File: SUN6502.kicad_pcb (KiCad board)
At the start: 4 copper layers, 221 x 179 mm, 52 parts, among them J1 Barrel_Jack_MountingPin, J2 6-5530843-5, J3 6-5530843-5, J4 DE9_Socket, SW1 RESET, SW2 Power Switch, U1 W65C02SxP, U10 MAX232, U11 74LS00, U2 KM62256CLP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

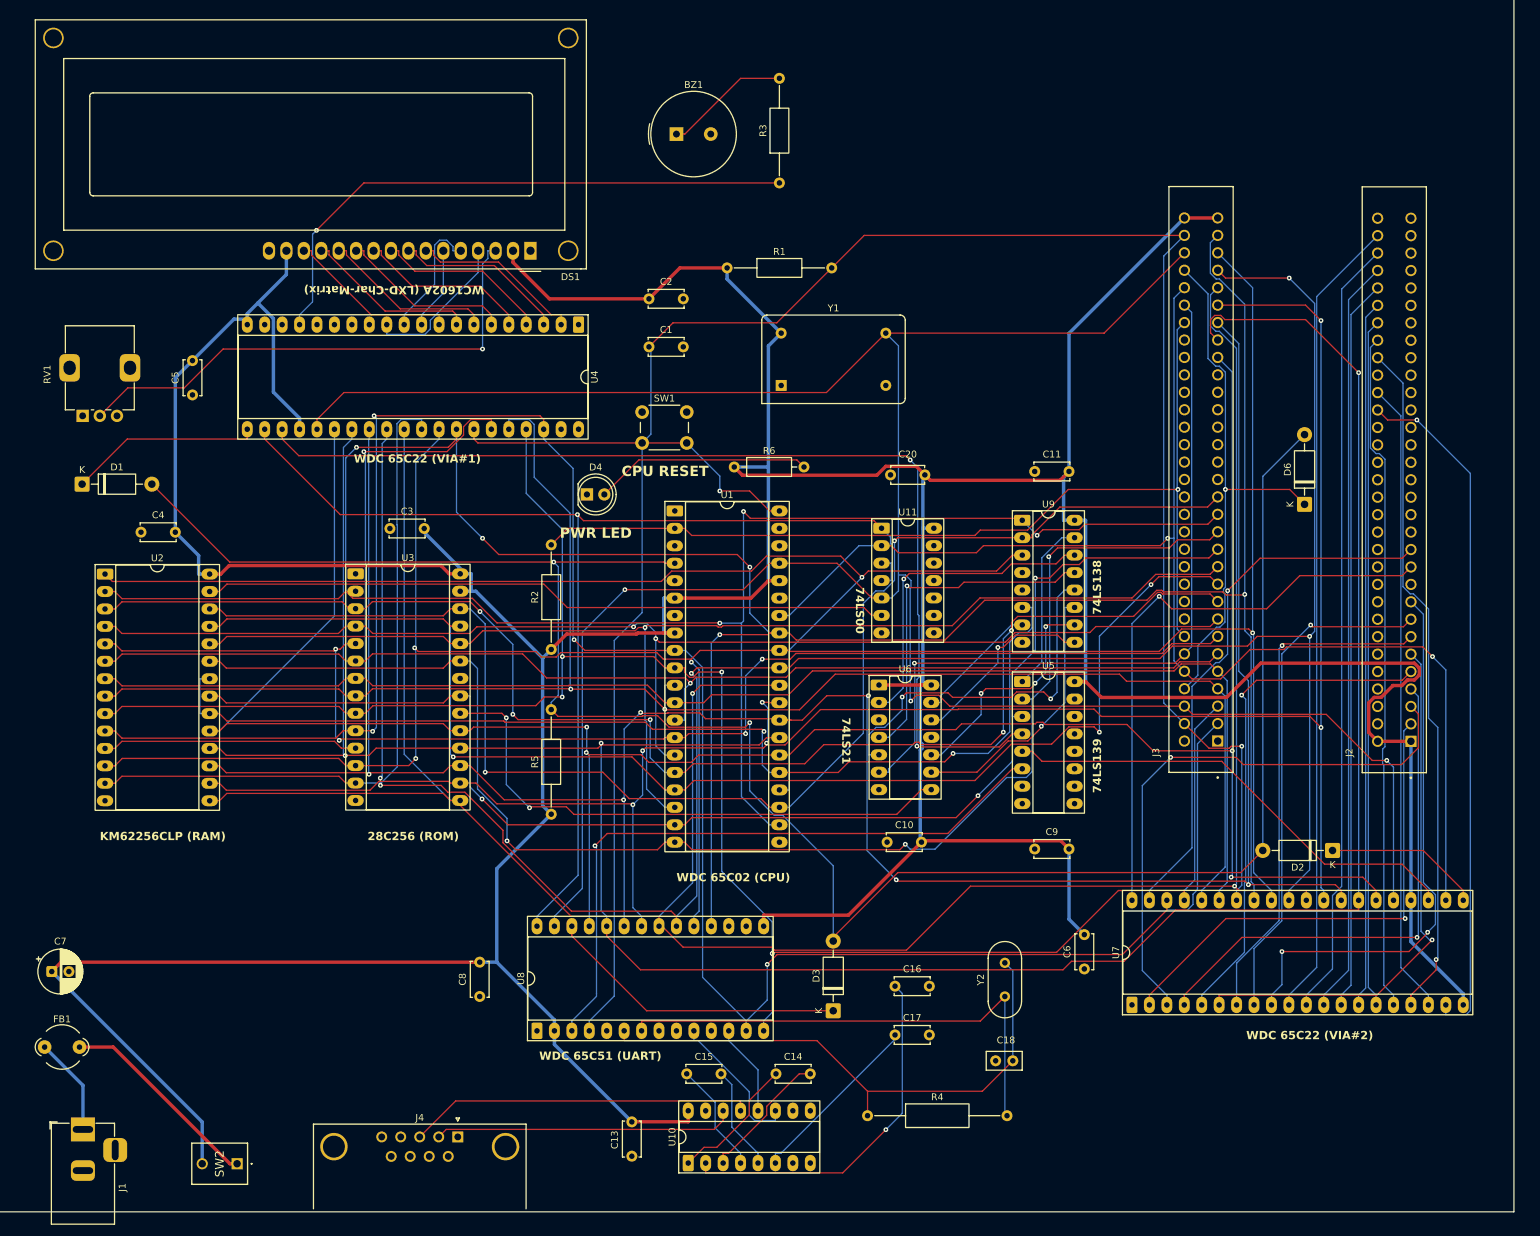
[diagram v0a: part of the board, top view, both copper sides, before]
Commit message: updates, changed ROM socket into ZIF
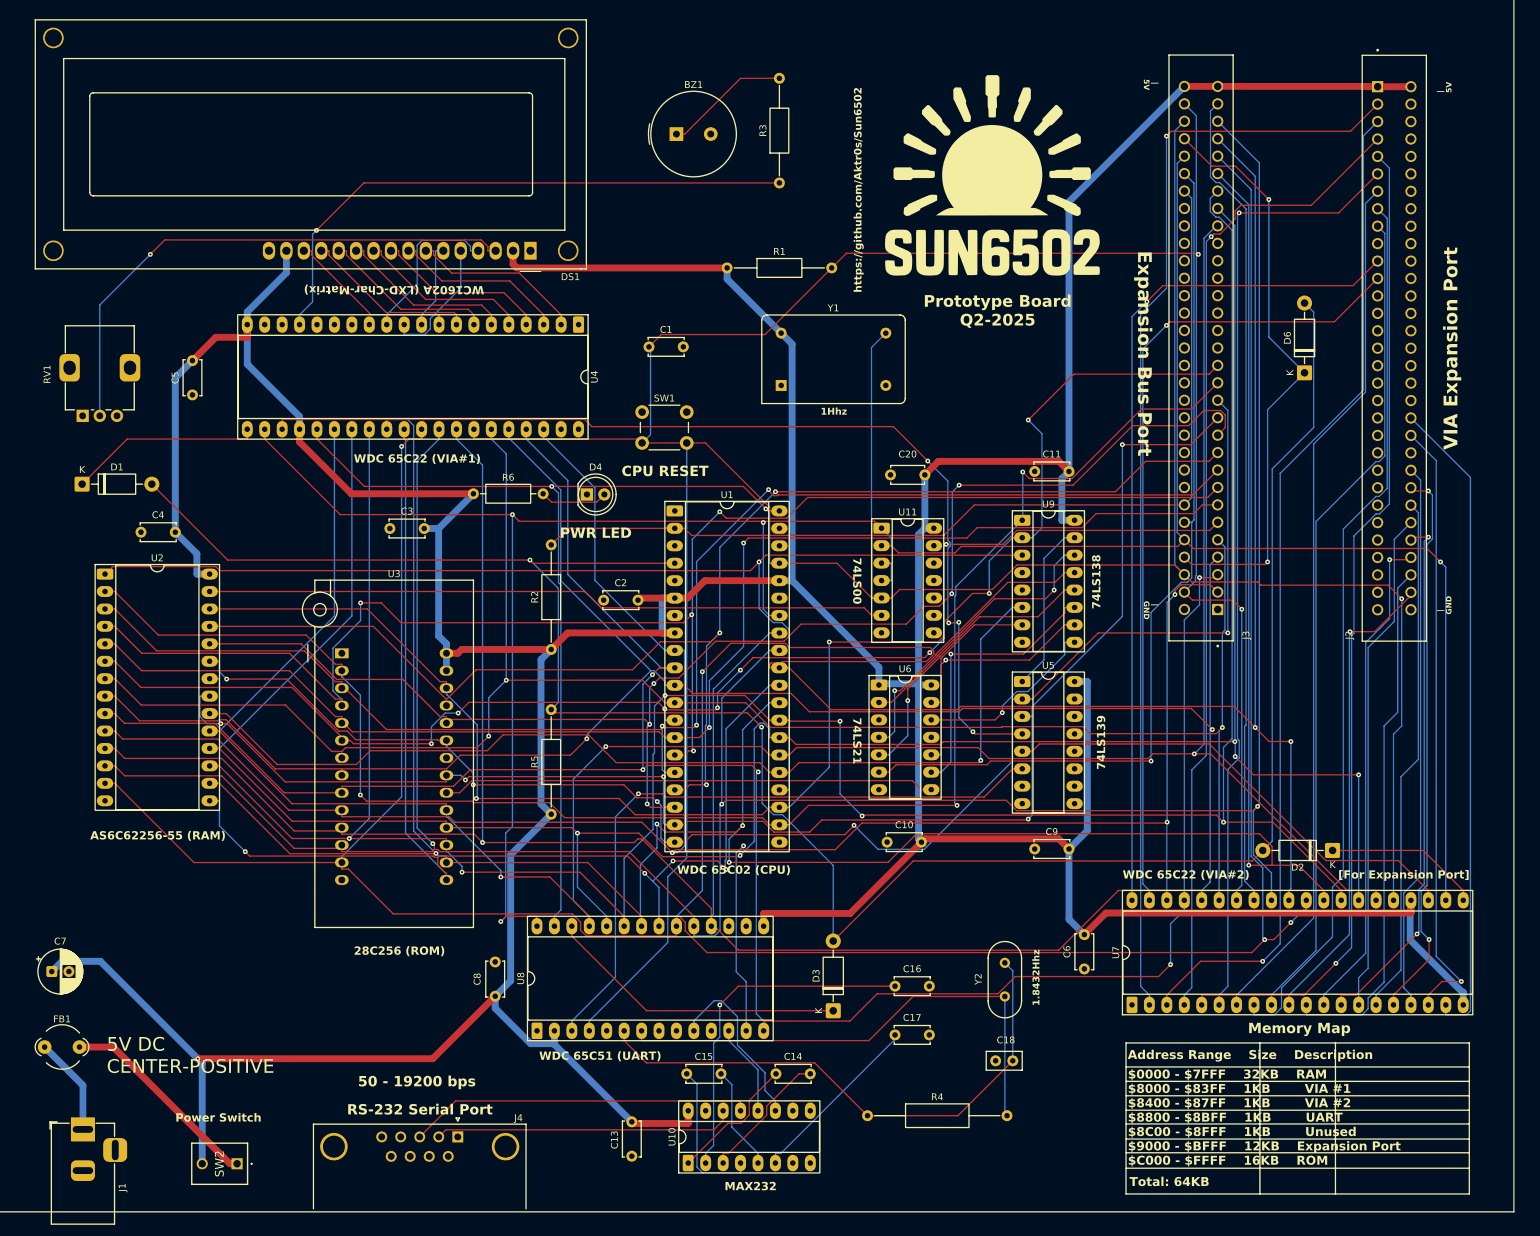
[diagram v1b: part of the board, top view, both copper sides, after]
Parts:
- added G***: LOGO, LOGO, F.Cu at (157.0, 41.0)
- U3: footprint Package_DIP:DIP-28_W15.24mm_Socket_LongPads -> Socket:DIP_Socket-28_W11.9_W12.7_W15.24_W17.78_W18.5_3M_228-1277-00-0602J
- moved C2 44.4 mm to (100.4, 101.9)
- moved R6 38.2 mm to (81.4, 86.4)
- moved D6 19.2 mm to (202.5, 68.8)
- moved J2 19.2 mm to (215.6, 65.2), turned to -90 degrees
- moved J3 19.2 mm to (187.4, 65.2)
- moved U3 11.8 mm to (62.3, 109.6)
- moved C8 5.52 mm to (84.6, 154.6), turned to -90 degrees
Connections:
- C2 pad 1: +5V -> GND
- C2 pad 2: GND -> +5V
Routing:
- net Net-(U7-PA0): track 72.2 -> 161.3 mm
- net Net-(U7-PA3): track 74.1 -> 144.7 mm
- net Net-(U7-PA2): track 75.5 -> 144.4 mm
- net /d2: track 388.8 -> 456.3 mm
- net Net-(U7-PA1): track 83.3 -> 146.7 mm
- net Net-(U7-PA4): track 78.9 -> 139.3 mm
- net Net-(U7-PA6): track 73.9 -> 129.5 mm, vias 1 -> 0
- net Net-(U7-PA5): track 74.4 -> 127.0 mm, vias 1 -> 0
- net /d1: track 358.8 -> 408.3 mm, vias 4 -> 3
- net Net-(U7-PB0): track 117.4 -> 69.6 mm, vias 0 -> 1
- net /d4: track 354.6 -> 399.6 mm, vias 7 -> 5
- net /a1: track 286.2 -> 328.8 mm, vias 4 -> 5
- net Net-(U7-PA7): track 80.9 -> 121.0 mm, vias 2 -> 0
- net Net-(U7-CA2): track 79.3 -> 119.2 mm
- net /d3: track 373.9 -> 413.8 mm, vias 2 -> 6
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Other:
- board text added: "$0000 - $7FFF 32KB RAM $8000 - $83FF 1KB VIA #1 $8400 - $87FF 1KB VIA #2 $8800 - $8BFF 1KB UART $8C00 - $8FFF 1KB Unused $9000 - $BFFF 12KB Expansion Port $C000 - $FFFF 16KB ROM"
- board text added: "1.8432Hhz"
- board text added: "1Hhz"
- board text added: "50 - 19200 bps"
- board text added: "5V DC CENTER-POSITIVE"
- board text added: "AS6C62256-55 (RAM)"
- board text added: "Address Range Size Description"
- board text added: "Expansion Bus Port"
- board text added: "MAX232"
- board text added: "Memory Map"
- board text added: "Power Switch"
- board text added: "Prototype Board Q2-2025"
- board text added: "RS-232 Serial Port"
- board text added: "Total: 64KB"
- board text added: "VIA Expansion Port"
- board text added: "[For Expansion Port]"
- board text added: "https://github.com/Aktr0s/Sun6502"
- board text added: "| 5V"
- board text added: "| GND"
- board text removed: "KM62256CLP (RAM)"

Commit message: pcb changed to 2 layers, CTR Added
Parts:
- R2, R5: value 1k -> 3.3k
- R3: value 1k -> 500
- moved C7 36.0 mm to (54.0, 167.9)
- moved FB1 5.39 mm to (17.6, 161.8)
- moved SW2 5.04 mm to (42.0, 184.1), turned to -90 degrees
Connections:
- J4 pad 8: unconnected-(J4-Pad8) -> Net-(U10-T2OUT)
- U10 pad 10: unconnected-(U10-T2IN-Pad10) -> Net-(U10-T2IN)
- U10 pad 7: unconnected-(U10-T2OUT-Pad7) -> Net-(U10-T2OUT)
- U4 pad 16: unconnected-(U4-PB6-Pad16) -> Net-(U10-T2IN)
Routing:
- net Net-(U10-T2IN): track 0.00 -> 255.3 mm, vias 0 -> 2
- net Net-(U10-T2OUT): track 0.00 -> 59.2 mm
- net /d2: track 456.3 -> 403.4 mm, vias 4 -> 3
- net GND: track 0.00 -> 35.1 mm, vias 0 -> 1
- net +5V: track 847.7 -> 816.7 mm, vias 1 -> 2
- net /d1: track 408.3 -> 430.0 mm, vias 3 -> 2
- net /d5: track 381.9 -> 360.6 mm, vias 6 -> 4
- net /a2: track 272.4 -> 292.7 mm, vias 2 -> 3
- net /a12: track 236.4 -> 254.5 mm
- net Net-(U7-PA1): track 146.7 -> 162.4 mm, vias 1 -> 2
- net Net-(U3-~{CS}): track 71.9 -> 87.6 mm
- net Net-(U7-PA0): track 161.3 -> 146.9 mm, vias 1 -> 0
- net /a15: track 153.8 -> 168.1 mm, vias 1 -> 2
- net /d6: track 365.8 -> 377.5 mm
- net /a0: track 318.9 -> 330.2 mm, vias 4 -> 5
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- removed copper zone on In1.Cu, net GND
- removed copper zone on In2.Cu, net GND
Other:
- copper layers 4 -> 2
- board text added: "1.8432MHz"
- board text added: "1MHz"
- board text added: "WC1602A (LCD-Char-Matrix)"
- board text removed: "1.8432Hhz"
- board text removed: "1Hhz"
- board text removed: "WC1602A (LXD-Char-Matrix)"

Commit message: small changes
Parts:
- C18: footprint Capacitor_THT:C_Disc_D5.0mm_W2.5mm_P2.50mm -> Capacitor_THT:C_Disc_D5.0mm_W2.5mm_P5.00mm
- R4: footprint Resistor_THT:R_Axial_DIN0309_L9.0mm_D3.2mm_P20.32mm_Horizontal -> Resistor_THT:R_Axial_DIN0207_L6.3mm_D2.5mm_P15.24mm_Horizontal
- Y2: footprint Crystal:Crystal_HC18-U_Vertical -> Crystal:Crystal_HC49-U_Vertical
- moved C18 2.50 mm to (155.0, 169.0)
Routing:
- net Net-(U10-T2IN): track 255.3 -> 248.1 mm
- net Net-(U8-XTAL2): track 73.3 -> 76.8 mm
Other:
- board text added: "6502 Hobby Computer"
- board text added: "WayWayWay"

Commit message: updates, board works
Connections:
- U11 pad 10: unconnected-(U11-Pad10) -> GND
- U11 pad 12: unconnected-(U11-Pad12) -> GND
- U11 pad 13: unconnected-(U11-Pad13) -> GND
- U11 pad 9: unconnected-(U11-Pad9) -> GND
- U5 pad 13: unconnected-(U5B-A1-Pad13) -> GND
- U5 pad 14: unconnected-(U5B-A0-Pad14) -> GND
- U5 pad 15: unconnected-(U5B-E-Pad15) -> GND
- U8 pad 16: unconnected-(U8-~{DCD}-Pad16) -> GND
- U8 pad 17: unconnected-(U8-~{DSR}-Pad17) -> GND
- U8 pad 9: unconnected-(U8-~{CTS}-Pad9) -> GND
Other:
- board text added: "$0000 - $7FFF 32KB RAM $8000 - $83FF 1KB VIA #1 $8400 - $87FF 1KB UART $8800 - $8BFF 1KB VIA #2 $8C00 - $8FFF 1KB Unused $9000 - $BFFF 12KB Expansion Port $C000 - $FFFF 16KB ROM"
- board text removed: "$0000 - $7FFF 32KB RAM $8000 - $83FF 1KB VIA #1 $8400 - $87FF 1KB VIA #2 $8800 - $8BFF 1KB UART $8C00 - $8FFF 1KB Unused $9000 - $BFFF 12KB Expansion Port $C000 - $FFFF 16KB ROM"
